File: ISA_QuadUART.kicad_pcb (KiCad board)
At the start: 2 copper layers, 104.1 x 102.9 mm, 41 parts, among them J1 ISA BUS, J11 Serial 4 IDC, J12 Serial 3 IDC, J13 UART4_SEL, J2 ADDR_IRQ, J3 UART1_SEL, J4 UART2_SEL, J5 ADDR, J6 Serial 2 IDC, J7 Serial 1 DB9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

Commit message: rerouted pcb
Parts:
- moved C5 1.91 mm to (217.2, 189.2)
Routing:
- net /A0: track 112.2 -> 153.1 mm, vias 1 -> 0
- net /~DCD_D: track 78.6 -> 44.5 mm
- net /~RI_D: track 52.7 -> 83.1 mm
- net /AEN: track 25.7 -> 53.7 mm
- net /RESETDRV: track 127.3 -> 100.7 mm, vias 1 -> 2
- net /~UART1_CS: track 87.6 -> 113.4 mm
- net /~IOW: track 100.1 -> 80.4 mm
- net /~DSR_C: track 45.1 -> 26.7 mm
- net /UARTB_IRQ: track 106.0 -> 89.2 mm
- net /0x2E8: track 55.3 -> 71.8 mm, vias 1 -> 0
- net /RX_D: track 47.2 -> 62.4 mm
- net /~DSR_D: track 53.7 -> 41.0 mm, vias 0 -> 1
- net /SER_CLK: track 28.5 -> 40.6 mm, vias 1 -> 0
- net /~UART2_CS: track 102.8 -> 93.4 mm, vias 0 -> 1
- net /A8: track 55.1 -> 45.8 mm, vias 1 -> 0
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
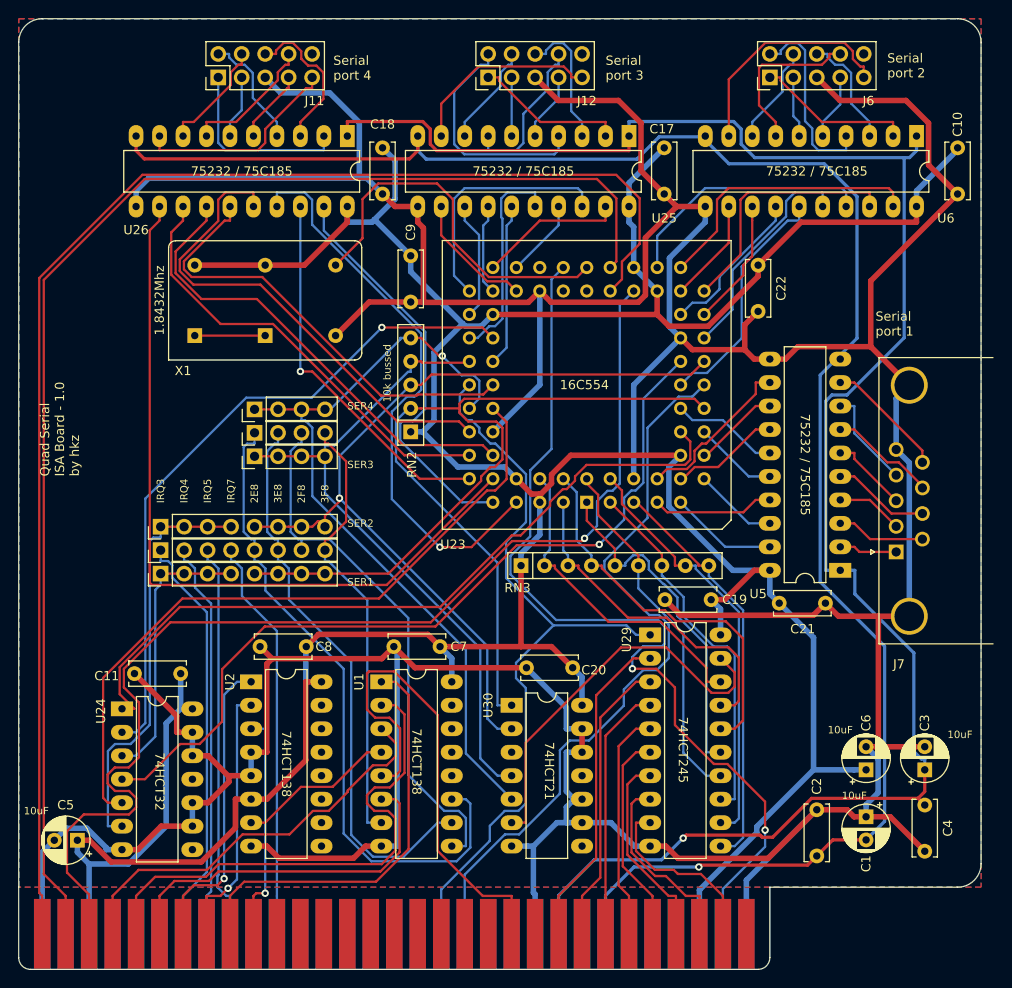
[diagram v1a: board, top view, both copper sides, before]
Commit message: Add 2 external serial ports
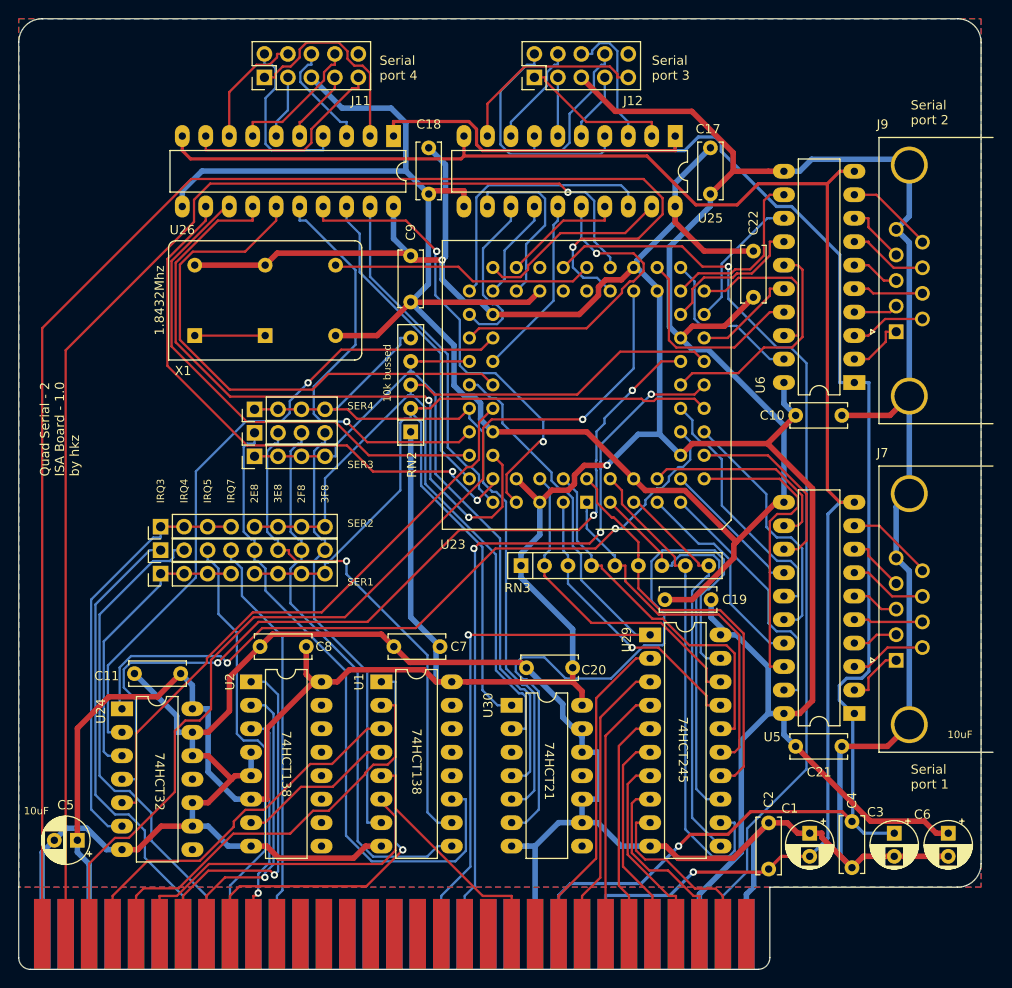
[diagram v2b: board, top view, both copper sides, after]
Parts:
- removed J6: Serial 2 IDC, Connector_PinHeader_2.54mm:PinHeader_2x05_P2.54mm_Vertical
- added J9: Serial 2 DB9, Connector_Dsub:DSUB-9_Male_Horizontal_P2.77x2.84mm_EdgePinOffset7.70mm_Housed_MountingHolesOffset9.12mm, F.Cu at (305.8, 134.2)
- moved C10 33.8 mm to (294.9, 143.3), turned to 0 degrees
- moved U6 27.5 mm to (301.2, 139.7), turned to 180 degrees
- moved C21 15.6 mm to (294.9, 179.1)
- moved U5 15.6 mm to (301.2, 175.5)
- moved J7 11.7 mm to (305.8, 169.8)
- moved C6 11.2 mm to (311.4, 188.5), turned to 270 degrees
- moved C4 8.07 mm to (301.0, 187.2)
- moved C3 7.61 mm to (305.6, 188.5), turned to 270 degrees
- moved C1 6.35 mm to (296.4, 188.5)
- moved C2 5.40 mm to (292.0, 187.3)
- moved C17 5.00 mm to (285.7, 114.3)
- moved C18 5.00 mm to (255.2, 114.3)
- moved J11 5.00 mm to (237.4, 106.7)
- moved J12 5.00 mm to (266.6, 106.7)
- moved U25 5.00 mm to (281.9, 113.0)
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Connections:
- J1 pad 11: (no net) -> /~MEMW
- J1 pad 12: (no net) -> /~MEMR
- J1 pad 15: (no net) -> Net-(J1-Pad15)
- J1 pad 16: (no net) -> Net-(J1-Pad16)
- J1 pad 17: (no net) -> Net-(J1-Pad17)
- J1 pad 18: (no net) -> Net-(J1-Pad18)
- J1 pad 19: (no net) -> Net-(J1-Pad19)
- J1 pad 20: (no net) -> Net-(J1-Pad20)
- J1 pad 22: (no net) -> /IRQ6
- J1 pad 26: (no net) -> /~DACK2
- J1 pad 27: (no net) -> /TC
- J1 pad 28: (no net) -> Net-(J1-Pad28)
- J1 pad 30: (no net) -> Net-(J1-Pad30)
- J1 pad 32: (no net) -> Net-(J1-Pad32)
- J1 pad 4: (no net) -> Net-(J1-Pad4)
- J1 pad 41: (no net) -> Net-(J1-Pad41)
- J1 pad 43: (no net) -> /A19
- J1 pad 44: (no net) -> /A18
- J1 pad 45: (no net) -> /A17
- J1 pad 46: (no net) -> /A16
- J1 pad 47: (no net) -> /A15
- J1 pad 48: (no net) -> /A14
- J1 pad 49: (no net) -> /A13
- J1 pad 5: (no net) -> Net-(J1-Pad5)
- J1 pad 50: (no net) -> /A12
- J1 pad 51: (no net) -> /A11
- J1 pad 52: (no net) -> /A10
- J1 pad 6: (no net) -> /DRQ2
- J1 pad 8: (no net) -> Net-(J1-Pad8)
- J11 pad 10: (no net) -> Net-(J11-Pad10)
- J12 pad 10: (no net) -> Net-(J12-Pad10)
- U1 pad 12: (no net) -> Net-(U1-Pad12)
- U1 pad 13: (no net) -> Net-(U1-Pad13)
- U1 pad 14: (no net) -> Net-(U1-Pad14)
- U1 pad 15: (no net) -> Net-(U1-Pad15)
- U2 pad 10: (no net) -> Net-(U2-Pad10)
- U2 pad 11: (no net) -> Net-(U2-Pad11)
- U2 pad 12: (no net) -> Net-(U2-Pad12)
- U2 pad 13: (no net) -> Net-(U2-Pad13)
- U2 pad 14: (no net) -> Net-(U2-Pad14)
- U2 pad 15: (no net) -> Net-(U2-Pad15)
- U2 pad 9: (no net) -> Net-(U2-Pad9)
- U23 pad 36: (no net) -> Net-(U23-Pad36)
- U23 pad 38: (no net) -> Net-(U23-Pad38)
- U23 pad 39: (no net) -> Net-(U23-Pad39)
- U24 pad 11: (no net) -> Net-(U24-Pad11)
- U24 pad 8: (no net) -> Net-(U24-Pad8)
- U30 pad 8: (no net) -> Net-(U30-Pad8)
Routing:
- net Net-(U29-Pad19): track 43.0 -> 71.3 mm
- net /AEN: track 53.7 -> 25.7 mm
- net +12V: track 202.3 -> 174.5 mm
- net /~DSR_A: track 9.11 -> 33.0 mm
- net /~CTS_D: track 51.1 -> 74.9 mm, vias 0 -> 2
- net /~RI_D: track 83.1 -> 61.8 mm, vias 0 -> 2
- net /A2: track 125.8 -> 107.3 mm
- net /~RTS_A: track 9.11 -> 27.3 mm
- net GND: track 589.6 -> 572.7 mm
- net /TX_A: track 11.7 -> 28.2 mm
- net /~DCD_A: track 11.7 -> 28.0 mm
- net /RS232_2_RX: track 20.8 -> 4.80 mm
- net /RS232_2_RI: track 25.1 -> 9.58 mm
- net VCC: track 411.4 -> 426.2 mm, vias 0 -> 2
- net /~UART1_CS: track 113.4 -> 99.8 mm
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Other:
- board text added: "Quad Serial - 2 ISA Board - 1.0 by hkz"
- board text removed: "16C554"
- board text removed: "75232 / 75C185"
- board text removed: "Quad Serial ISA Board - 1.0 by hkz"

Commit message: Fix silkscreen
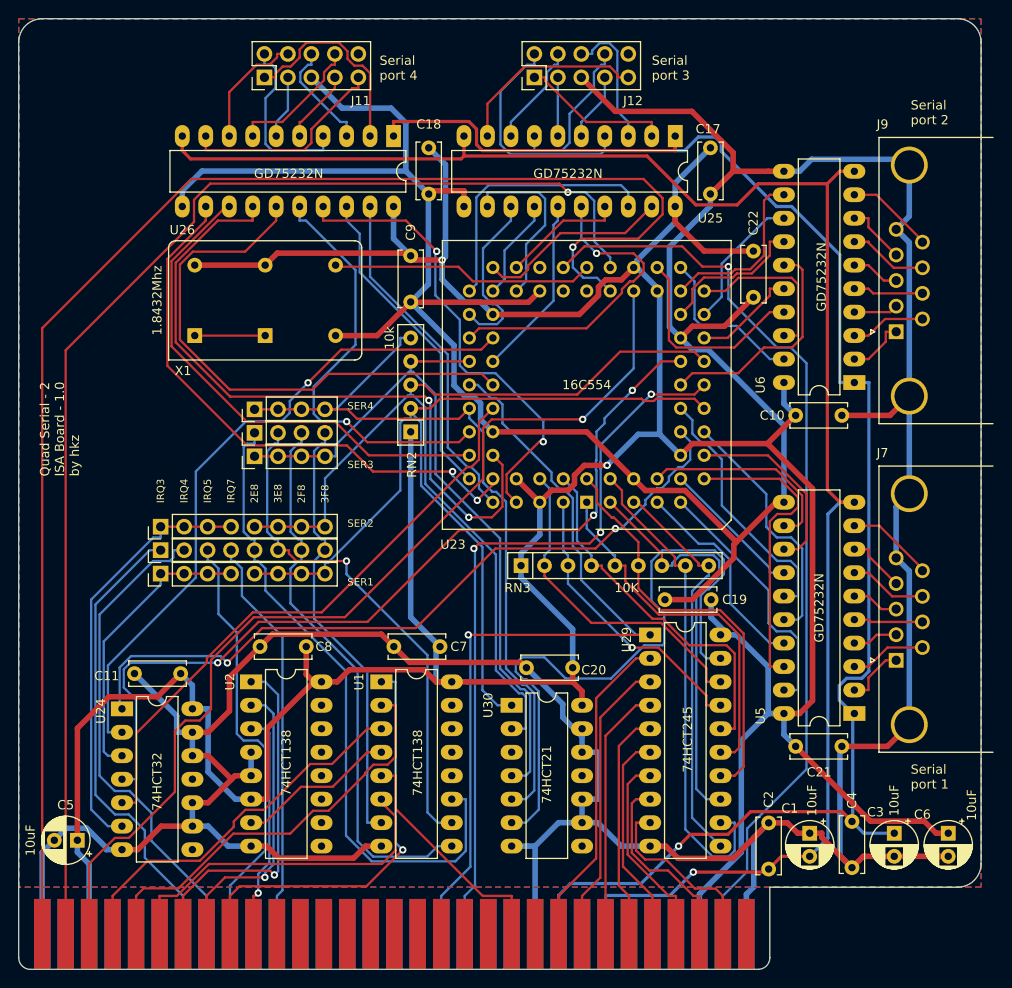
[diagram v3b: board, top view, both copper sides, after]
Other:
- board text removed: "1.8432Mhz"
- board text removed: "10k bussed"
- board text removed: "10uF"
- board text removed: "74HCT138"
- board text removed: "74HCT21"
- board text removed: "74HCT245"
- board text removed: "74HCT32"
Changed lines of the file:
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@@
   (general
     (thickness 1.6)
-    (drawings 40)
+    (drawings 30)
     (tracks 1380)
     (zones 0)
@@
       (effects (font (size 1 1) (thickness 0.15)))
     )
-    (fp_text value 74HCT21 (at 3.81 17.57) (layer F.Fab)
+    (fp_text value 74HCT21 (at 3.81 7.493 90) (layer F.SilkS)
       (effects (font (size 1 1) (thickness 0.15)))
     )
@@
       (effects (font (size 1 1) (thickness 0.15)))
     )
-    (fp_text value 10K (at 11.43 2.4) (layer F.Fab)
+    (fp_text value 10K (at 11.43 2.4) (layer F.SilkS)
       (effects (font (size 1 1) (thickness 0.15)))
     )
@@
       (effects (font (size 1 1) (thickness 0.15)))
     )
-    (fp_text value 74HCT245 (at 3.81 25.19) (layer F.Fab)
+    (fp_text value 74HCT245 (at 4.064 11.303 90) (layer F.SilkS)
       (effects (font (size 1 1) (thickness 0.15)))
     )
@@
       (effects (font (size 1 1) (thickness 0.15)))
     )
-    (fp_text value GD75232N (at 3.81 25.19 90) (layer F.Fab)
+    (fp_text value GD75232N (at 4.064 11.35) (layer F.SilkS)
       (effects (font (size 1 1) (thickness 0.15)))
     )
@@
       (effects (font (size 1 1) (thickness 0.15)))
     )
-    (fp_text value GD75232N (at 3.81 25.19 90) (layer F.Fab)
+    (fp_text value GD75232N (at 4.064 11.604) (layer F.SilkS)
       (effects (font (size 1 1) (thickness 0.15)))
     )
@@
       (effects (font (size 1 1) (thickness 0.15)))
     )
-    (fp_text value 74HCT32 (at 3.81 17.57) (layer F.Fab)
+    (fp_text value 74HCT32 (at 3.81 7.874 90) (layer F.SilkS)
       (effects (font (size 1 1) (thickness 0.15)))
     )
@@
       (effects (font (size 1 1) (thickness 0.15)))
     )
-    (fp_text value 16C554 (at 0 29.225) (layer F.Fab)
+    (fp_text value 16C554 (at 0 12.7) (layer F.SilkS)
       (effects (font (size 1 1) (thickness 0.15)))
     )
@@
     (descr "20-lead though-hole mounted DIP package, row spacing 7.62 mm (300 mils), LongPads")
     (tags "THT DIP DIL PDIP 2.54mm 7.62mm 300mil LongPads")
-    (fp_text reference U5 (at 8.89 -2.54) (layer F.SilkS)
+    (fp_text reference U5 (at 10.16 -0.254 -90) (layer F.SilkS)
       (effects (font (size 1 1) (thickness 0.15)))
     )
-    (fp_text value GD75232N (at 3.81 25.19) (layer F.Fab)
+    (fp_text value GD75232N (at 3.81 11.43 -90) (layer F.SilkS)
       (effects (font (size 1 1) (thickness 0.15)))
     )
@@
       (effects (font (size 1 1) (thickness 0.15)))
     )
-    (fp_text value 10k (at 6.35 2.4 90) (layer F.Fab)
+    (fp_text value 10k (at 10.16 -2.286 90) (layer F.SilkS)
       (effects (font (size 1 1) (thickness 0.15)))
     )
@@
       (effects (font (size 1 1) (thickness 0.15)))
     )
-    (fp_text value 1.8432Mhz (at 7.62 3.74) (layer F.Fab)
+    (fp_text value 1.8432Mhz (at -4.064 -3.81 90) (layer F.SilkS)
       (effects (font (size 1 1) (thickness 0.15)))
     )
@@
     (descr "20-lead though-hole mounted DIP package, row spacing 7.62 mm (300 mils), LongPads")
     (tags "THT DIP DIL PDIP 2.54mm 7.62mm 300mil LongPads")
-    (fp_text reference U6 (at 10.16 -0.254 90) (layer F.SilkS)
+    (fp_text reference U6 (at 10.16 -0.254 -90) (layer F.SilkS)
       (effects (font (size 1 1) (thickness 0.15)))
     )
-    (fp_text value GD75232N (at 3.81 25.19) (layer F.Fab)
+    (fp_text value GD75232N (at 3.556 11.43 -90) (layer F.SilkS)
       (effects (font (size 1 1) (thickness 0.15)))
     )
@@
       (effects (font (size 1 1) (thickness 0.15)))
     )
-    (fp_text value 74HCT138 (at 3.81 20.11) (layer F.Fab)
+    (fp_text value 74HCT138 (at 3.81 8.763 90) (layer F.SilkS)
       (effects (font (size 1 1) (thickness 0.15)))
     )
@@
       (effects (font (size 1 1) (thickness 0.15)))
     )
-    (fp_text value 74HCT138 (at 3.81 20.11) (layer F.Fab)
+    (fp_text value 74HCT138 (at 3.937 8.763 90) (layer F.SilkS)
       (effects (font (size 1 1) (thickness 0.15)))
     )
@@
       (effects (font (size 1 1) (thickness 0.15)))
     )
-    (fp_text value 10uF (at 1.25 3.75 90) (layer F.Fab)
+    (fp_text value 10uF (at -3.048 -2.54 90) (layer F.SilkS)
       (effects (font (size 1 1) (thickness 0.15)))
     )
@@
       (effects (font (size 1 1) (thickness 0.15)))
     )
-    (fp_text value 10uF (at 1.25 3.75) (layer F.Fab)
+    (fp_text value 10uF (at 5.08 0 90) (layer F.SilkS)
       (effects (font (size 1 1) (thickness 0.15)))
     )
@@
       (effects (font (size 1 1) (thickness 0.15)))
     )
-    (fp_text value 10uF (at 1.25 3.75 90) (layer F.Fab)
+    (fp_text value 10uF (at -3.556 0 90) (layer F.SilkS)
       (effects (font (size 1 1) (thickness 0.15)))
     )
@@
       (effects (font (size 1 1) (thickness 0.15)))
     )
-    (fp_text value 10uF (at 1.25 3.75 90) (layer F.Fab)
+    (fp_text value 10uF (at -3.556 -0.254 90) (layer F.SilkS)
       (effects (font (size 1 1) (thickness 0.15)))
     )
@@
     (effects (font (size 1 1) (thickness 0.25)) (justify left))
   )
-  (gr_text 74HCT21 (at 268.224 181.737 -90) (layer F.SilkS)
-    (effects (font (size 1 1) (thickness 0.15)))
-  )
-  (gr_text 74HCT245 (at 282.702 179.451 -90) (layer F.SilkS)
-    (effects (font (size 1 1) (thickness 0.15)))
-  )
-  (gr_text "10k bussed" (at 250.698 138.684 90) (layer F.SilkS)
-    (effects (font (size 0.8 0.8) (thickness 0.2)))
-  )
   (gr_text SER4 (at 246.38 142.24) (layer F.SilkS)
     (effects (font (size 0.8 0.8) (thickness 0.15)) (justify left))
@@
     (effects (font (size 0.8 0.8) (thickness 0.15)) (justify left))
   )
-  (gr_text 74HCT32 (at 226.06 182.88 -90) (layer F.SilkS)
-    (effects (font (size 1 1) (thickness 0.15)))
-  )
   (gr_text "Serial\nport 4" (at 249.856 105.664) (layer F.SilkS)
     (effects (font (size 1 1) (thickness 0.25)) (justify left))
@@
     (effects (font (size 1 1) (thickness 0.25)) (justify left))
   )
-  (gr_text 10uF (at 312.674 177.8) (layer F.SilkS)
-    (effects (font (size 0.8 0.8) (thickness 0.15)))
-  )
-  (gr_text 10uF (at 212.725 186.055) (layer F.SilkS)
-    (effects (font (size 0.8 0.8) (thickness 0.15)))
-  )
-  (gr_text 1.8432Mhz (at 226.06 130.81 90) (layer F.SilkS)
-    (effects (font (size 1 1) (thickness 0.15)))
-  )
   (gr_text "Serial\nport 1" (at 307.34 182.372) (layer F.SilkS)
     (effects (font (size 1 1) (thickness 0.25)) (justify left))
   )
-  (gr_text 74HCT138 (at 239.776 180.975 -90) (layer F.SilkS)
-    (effects (font (size 1 1) (thickness 0.15)))
-  )
-  (gr_text 74HCT138 (at 253.873 180.721 -90) (layer F.SilkS)
-    (effects (font (size 1 1) (thickness 0.15)))
-  )
   (gr_text 3F8 (at 243.96 152.76 90) (layer F.SilkS)
     (effects (font (size 0.8 0.8) (thickness 0.15)) (justify left))
@@
   (gr_arc (start 290.83 201.93) (end 290.83 203.2) (angle -90) (layer Edge.Cuts) (width 0.05))
   (gr_arc (start 312.42 191.77) (end 312.42 194.31) (angle -90) (layer Edge.Cuts) (width 0.05))
-  (dimension 6.35 (width 0.15) (layer Dwgs.User)
-    (gr_text "6,350 mm" (at 311.785 166.4) (layer Dwgs.User)
-      (effects (font (size 1 1) (thickness 0.15)))
-    )
-    (feature1 (pts (xy 308.61 157.48) (xy 308.61 165.686421)))
-    (feature2 (pts (xy 314.96 157.48) (xy 314.96 165.686421)))
-    (crossbar (pts (xy 314.96 165.1) (xy 308.61 165.1)))
-    (arrow1a (pts (xy 308.61 165.1) (xy 309.736504 164.513579)))
-    (arrow1b (pts (xy 308.61 165.1) (xy 309.736504 165.686421)))
-    (arrow2a (pts (xy 314.96 165.1) (xy 313.833496 164.513579)))
-    (arrow2b (pts (xy 314.96 165.1) (xy 313.833496 165.686421)))
-  )
   (dimension 22.86 (width 0.15) (layer Dwgs.User)
     (gr_text "22,860 mm" (at 303.53 200.69) (layer Dwgs.User)

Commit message: Move connectors
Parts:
- moved C4 73.8 mm to (289.3, 114.3)
- moved C3 73.0 mm to (301.8, 115.6)
- moved C1 72.9 mm to (295.9, 115.6)
- moved C2 62.7 mm to (294.9, 124.7), turned to 0 degrees
- moved C6 24.4 mm to (287.0, 190.2), turned to 0 degrees
- moved J7 12.1 mm to (305.8, 181.9)
- moved J9 12.1 mm to (305.8, 146.3)
- moved U6 12.1 mm to (301.2, 151.8)
- moved C10 12.1 mm to (294.9, 155.4)
- moved C21 12.1 mm to (294.9, 191.2)
- moved U5 12.1 mm to (301.2, 187.6)
- moved U29 3.98 mm to (275.3, 168.2)
- moved C19 3.94 mm to (281.9, 164.2)
- moved U30 2.79 mm to (261.6, 175.8)
- moved C20 2.65 mm to (268.2, 171.3)
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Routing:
- net Net-(U29-Pad19): track 71.3 -> 34.7 mm
- net /~RTS_A: track 27.3 -> 61.1 mm
- net /UARTD_IRQ: track 64.8 -> 90.2 mm, vias 0 -> 1
- net /A1: track 138.0 -> 113.4 mm, vias 1 -> 2
- net /RESETDRV: track 100.1 -> 120.4 mm, vias 1 -> 0
- net /~IOW: track 80.1 -> 99.0 mm, vias 3 -> 1
- net /TX_D: track 59.3 -> 41.4 mm
- net VCC: track 426.2 -> 408.4 mm, vias 2 -> 1
- net /A3: track 41.1 -> 57.2 mm
- net /0x2E8: track 71.3 -> 55.3 mm, vias 0 -> 1
- net /~DCD_A: track 28.0 -> 42.3 mm
- net /~IOR: track 90.6 -> 76.9 mm, vias 1 -> 0
- net /TX_B: track 24.8 -> 11.7 mm
- net /~CTS_A: track 15.7 -> 27.8 mm
- net /~UART1_CS: track 99.8 -> 88.0 mm
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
